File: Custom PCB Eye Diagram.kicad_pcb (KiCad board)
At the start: 4 copper layers, 82.8 x 100.2 mm, 49 parts, among them IC1 CLK DSC1123CI2-125.0000, J1 RD53 Data Lines DP 47272-0001, J10 JTAG Connector 0878321420, J11 12v Input PJ-102B, J12 LVDS Pair-P Conn_01x02, J13 LVDS Pair-N Conn_01x02, J14 MGT CLK-P Conn_01x01, J15 MGT CLK-N Conn_01x01, J16 Ground Pin Conn_01x04, J17 Ground Pins Conn_01x04, J2 Conn_01x02, J3 LSHM-1 LSHM-150-XX.X-XX-DV-A-N, J4 Loopback DP 47272-0001, J5 LSHM-2 LSHM-150-XX.X-XX-DV-A-N, J6 Vin Conn_01x03, J7 Conn_01x02, J8 LVDS-N Conn_01x02, J9 LVDS-P Conn_01x02, U1 DCDC Convertor 12v to 3.3v OKI-78SR-3.3_1.5-W36-C

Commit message: Added test LEDs for practicing FPGA programming
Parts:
- added D2: LED, LED_SMD:LED_0603_1608Metric, F.Cu at (147.3, 97.6)
- added D3: LED, LED_SMD:LED_0603_1608Metric, F.Cu at (143.8, 79.2)
- added D4: LED, LED_SMD:LED_0603_1608Metric, F.Cu at (146.8, 79.1)
- added R5: R, Resistor_SMD:R_0402_1005Metric, F.Cu at (147.3, 93.9)
- added R6: R, Resistor_SMD:R_0402_1005Metric, F.Cu at (143.8, 83.5)
- added R7: R, Resistor_SMD:R_0402_1005Metric, F.Cu at (146.8, 82.3)
- C7: renamed from C7 VIn
- D1: renamed from D1 Power Light
- IC1: renamed from IC1 CLK
- J1: renamed from J1 RD53 Data Lines DP
- J10: renamed from J10 JTAG Connector
- J11: renamed from J11 12v Input
- J12: renamed from J12 LVDS Pair-P
- J13: renamed from J13 LVDS Pair-N
- J14: renamed from J14 MGT CLK-P
- J15: renamed from J15 MGT CLK-N
- J16: renamed from J16 Ground Pin
- J17: renamed from J17 Ground Pins
- J3: renamed from J3 LSHM-1
- J4: renamed from J4 Loopback DP
- J5: renamed from J5 LSHM-2
- J6: renamed from J6 Vin
- J8: renamed from J8 LVDS-N
- J9: renamed from J9 LVDS-P
- U1: renamed from U1 DCDC Convertor 12v to 3.3v
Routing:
- net GND: track 96.0 -> 102.0 mm, vias 15 -> 18
- net Net-(J3-Pad56): track 0.00 -> 3.83 mm
- net Net-(J3-Pad53): track 0.00 -> 3.12 mm
- net Net-(D3-Pad2): track 0.00 -> 3.03 mm
- net Net-(J3-Pad68): track 0.00 -> 2.64 mm
- net Net-(D2-Pad2): track 0.00 -> 2.42 mm
- net Net-(D4-Pad2): track 0.00 -> 1.89 mm

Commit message: Fixed test LED setup for FPGA programming practice
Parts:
- removed D2, D3, D4: LED, LED_SMD:LED_0603_1608Metric
- removed J7: Conn_01x02, Connector_PinHeader_2.54mm:PinHeader_1x02_P2.54mm_Vertical
- added 50 D2: LED, LED_SMD:LED_0603_1608Metric, F.Cu at (119.3, 72.0)
- added 56 D4: LED, LED_SMD:LED_0603_1608Metric, F.Cu at (119.3, 73.7)
- added 66 D9: LED, LED_SMD:LED_0603_1608Metric, F.Cu at (119.3, 75.5)
- added 68 D3: LED, LED_SMD:LED_0603_1608Metric, F.Cu at (119.3, 77.4)
- added 74 D5: LED, LED_SMD:LED_0603_1608Metric, F.Cu at (119.3, 79.1)
- added 78 D6: LED, LED_SMD:LED_0603_1608Metric, F.Cu at (119.3, 80.9)
- added 82 D7: LED, LED_SMD:LED_0603_1608Metric, F.Cu at (119.3, 82.5)
- added 88 D8: LED, LED_SMD:LED_0603_1608Metric, F.Cu at (119.2, 84.3)
- added J7 VIN: Conn_01x02, Connector_PinHeader_2.54mm:PinHeader_1x02_P2.54mm_Vertical, F.Cu at (202.6, 93.1)
- added R10: R, Resistor_SMD:R_0402_1005Metric, F.Cu at (140.8, 79.2)
- added R11: R, Resistor_SMD:R_0402_1005Metric, F.Cu at (139.7, 80.7)
- added R12: R, Resistor_SMD:R_0402_1005Metric, F.Cu at (138.3, 82.2)
- added R8: R, Resistor_SMD:R_0402_1005Metric, F.Cu at (143.8, 75.0)
- added R9: R, Resistor_SMD:R_0402_1005Metric, F.Cu at (141.8, 77.6)
- D1 Power LED: renamed from D1
- IC1 MGT_CLK circuit from FPGA: renamed from IC1
- J1 SCC GRX Signals: renamed from J1
- J10 JTAG Connector: renamed from J10
- J11 12v Power Input: renamed from J11
- J12 LVDS_P: renamed from J12
- J13 LVDS_N: renamed from J13
- J14 MGT_CLK_P: renamed from J14
- J15 MGT_CLK_N: renamed from J15
- J16 Ground Pins: renamed from J16
- J17 Ground Pins: renamed from J17
- J2 12v: renamed from J2
- J3 LSHM Connector to FPGA: renamed from J3
- J4 GTX Signals for Loopback: renamed from J4
- J5 Added for Stability: renamed from J5
- J6 VIN: renamed from J6
- J8 LVDS_N: renamed from J8
- J9 LVDS_P: renamed from J9
- U1 12v to 3.3v DCDC Converter: renamed from U1
- moved J16 Ground Pins 30.5 mm to (172.1, 147.1)
- moved R5 21.9 mm to (147.8, 72.0), turned to 180 degrees
- moved R7 8.73 mm to (146.2, 73.6), turned to 0 degrees
- moved J11 12v Power Input 7.76 mm to (120.3, 124.9)
- moved R6 7.02 mm to (143.0, 76.5), turned to 0 degrees
- moved REF** 6.50 mm to (121.6, 145.7)
- moved REF** 6.50 mm to (121.6, 55.5)
- moved C7 4.80 mm to (129.2, 86.0)
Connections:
- FB1 pad 2: +3V3 -> /VIN
- R5 pad 1: Net-(J3-Pad53) -> Net-(J3-Pad50)
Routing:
- net Net-(D2-Pad2): track 2.42 -> 27.3 mm
- net Net-(D4-Pad2): track 1.89 -> 25.8 mm
- net Net-(D9-Pad2): track 0.00 -> 23.4 mm
- net Net-(D5-Pad2): track 0.00 -> 21.9 mm
- net Net-(D6-Pad2): track 0.00 -> 20.9 mm
- net Net-(D7-Pad2): track 0.00 -> 19.9 mm
- net Net-(D3-Pad2): track 3.03 -> 22.8 mm
- net Net-(D8-Pad2): track 0.00 -> 18.6 mm
- net Net-(J3-Pad50): track 0.00 -> 14.7 mm
- net Net-(J3-Pad66): track 0.00 -> 11.7 mm
- net GND: track 102.0 -> 111.5 mm, vias 18 -> 16
- net Net-(J3-Pad56): track 3.83 -> 13.1 mm
- net Net-(J3-Pad74): track 0.00 -> 8.96 mm
- net +12V: track 30.8 -> 38.5 mm
- net Net-(J3-Pad68): track 2.64 -> 10.2 mm
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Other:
- board size 82.8 x 100.2 mm -> 89.3 x 100.2 mm

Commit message: Added LBNL logo, name, and changed VIN layer to V3P3 layer
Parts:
- added G***: LOGO, lbnl_logo:lbnl_logo_large, F.Cu at (144.2, 144.7)
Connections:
- C7 pad 1: /VIN -> /V3P3
- C8 pad 2: /VIN -> /V3P3
- FB1 pad 2: /VIN -> /V3P3
- IC1 MGT_CLK circuit from FPGA pad 1: /VIN -> /V3P3
- J3 LSHM Connector to FPGA pad 100: /VIN -> /V3P3
- J3 LSHM Connector to FPGA pad 98: /VIN -> /V3P3
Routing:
- net /VIN: track 18.7 -> 0.00 mm, vias 3 -> 0
- net /V3P3: track 0.00 -> 18.7 mm, vias 0 -> 3
- added copper zone on In2.Cu, net /V3P3
- removed copper zone on In2.Cu, net /VIN
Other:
- board text added: "RD53B Digital Signal Eye Diagram PCB 1.0 Adam Molnar August 24 2020"

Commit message: Another iteration of the PCB and made some updates to the BOM
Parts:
- removed 50 D2: LED, LED_SMD:LED_0603_1608Metric
- removed 56 D4: LED, LED_SMD:LED_0603_1608Metric
- removed 66 D9: LED, LED_SMD:LED_0603_1608Metric
- removed 68 D3: LED, LED_SMD:LED_0603_1608Metric
- removed 74 D5: LED, LED_SMD:LED_0603_1608Metric
- removed 78 D6: LED, LED_SMD:LED_0603_1608Metric
- removed 82 D7: LED, LED_SMD:LED_0603_1608Metric
- removed 88 D8: LED, LED_SMD:LED_0603_1608Metric
- removed the C10 at (196.6, 108.5)
- removed the C6 at (198.9, 104.8)
- removed the C9 at (139.5, 129.4)
- removed D1 Power LED: LED, LED_SMD:LED_0603_1608Metric
- removed J11 12v Power Input: PJ-102B, PJ-102B:CUI_PJ-102B
- removed J14 MGT_CLK_P: Conn_01x01, Connector_PinHeader_2.54mm:PinHeader_1x01_P2.54mm_Vertical
- removed J15 MGT_CLK_N: Conn_01x01, Connector_PinHeader_2.54mm:PinHeader_1x01_P2.54mm_Vertical
- removed J16 Ground Pins: Conn_01x04, Connector_PinHeader_2.54mm:PinHeader_1x04_P2.54mm_Vertical
- removed J17 Ground Pins: Conn_01x04, Connector_PinHeader_2.54mm:PinHeader_1x04_P2.54mm_Vertical
- removed J2 12v: Conn_01x02, Connector_PinHeader_2.54mm:PinHeader_1x02_P2.54mm_Vertical
- removed J6 VIN: Conn_01x03, Connector_PinHeader_2.54mm:PinHeader_1x03_P2.54mm_Vertical
- removed the R3 at (176.6, 100.2)
- removed REF** (x4): MountingHole_3.2mm_M3, MountingHole:MountingHole_3.2mm_M3
- removed U1 12v to 3.3v DCDC Converter: OKI-78SR-3.3_1.5-W36-C, Converter_DCDC:Converter_DCDC_RECOM_R-78B-2.0_THT
- added 3.2mm: MountingHole_3.2mm_M3, MountingHole:MountingHole_3.2mm_M3, F.Cu at (200.8, 145.7)
- added 3.2mm : MountingHole_3.2mm_M3, MountingHole:MountingHole_3.2mm_M3, F.Cu at (120.6, 55.5)
- added 3.2mm: MountingHole_3.2mm_M3, MountingHole:MountingHole_3.2mm_M3, F.Cu at (200.8, 55.5)
- added 3.2mm: MountingHole_3.2mm_M3, MountingHole:MountingHole_3.2mm_M3, F.Cu at (120.6, 145.7)
- added C1: 10UF, Capacitor_SMD:C_0805_2012Metric, F.Cu at (150.2, 121.3)
- added C5: 10UF, Capacitor_SMD:C_0805_2012Metric, F.Cu at (131.6, 136.7)
- added C7: 470n, Capacitor_SMD:C_0805_2012Metric, F.Cu at (180.8, 108.0)
- added D1: LED, LED_SMD:LED_0603_1608Metric, F.Cu at (156.6, 129.0)
- added D2: LED, LED_SMD:LED_0603_1608Metric, F.Cu at (119.3, 79.1)
- added D3: LED, LED_SMD:LED_0603_1608Metric, F.Cu at (119.3, 80.9)
- added D4: LED, LED_SMD:LED_0603_1608Metric, F.Cu at (119.3, 82.5)
- added D5: LED, LED_SMD:LED_0603_1608Metric, F.Cu at (119.2, 84.3)
- added D6: LED, LED_SMD:LED_0603_1608Metric, F.Cu at (119.3, 72.0)
- added D7: LED, LED_SMD:LED_0603_1608Metric, F.Cu at (119.3, 77.4)
- added D8: LED, LED_SMD:LED_0603_1608Metric, F.Cu at (119.3, 73.7)
- added D9: LED, LED_SMD:LED_0603_1608Metric, F.Cu at (119.3, 75.5)
- added J1: Conn_01x02, Connector_PinHeader_2.54mm:PinHeader_1x02_P2.54mm_Vertical, F.Cu at (130.9, 118.8)
- added J10: PJ-102B, PJ-102B:CUI_PJ-102B, F.Cu at (118.2, 132.6)
- added J15: Conn_01x02, Connector_PinHeader_2.54mm:PinHeader_1x02_P2.54mm_Vertical, F.Cu at (168.7, 101.3)
- added J17: Conn_01x02, Connector_PinHeader_2.54mm:PinHeader_1x02_P2.54mm_Vertical, F.Cu at (158.6, 118.0)
- added J2: Conn_01x04, Connector_PinHeader_2.54mm:PinHeader_1x04_P2.54mm_Vertical, F.Cu at (172.1, 147.1)
- added J3: Conn_01x03, Connector_PinHeader_2.54mm:PinHeader_1x03_P2.54mm_Vertical, F.Cu at (143.9, 118.8)
- added J5: Conn_01x04, Connector_PinHeader_2.54mm:PinHeader_1x04_P2.54mm_Vertical, F.Cu at (145.2, 54.2)
- added R2: 200, Resistor_SMD:R_0603_1608Metric, F.Cu at (157.4, 124.8)
- added U1: OKI-78SR-3.3_1.5-W36-C, Converter_DCDC:Converter_DCDC_RECOM_R-78B-2.0_THT, F.Cu at (137.2, 134.1)
- C3: value 470n -> 10UF
- IC1: renamed from IC1 MGT_CLK circuit from FPGA
- J11: renamed from J12 LVDS_P
- J12: renamed from J13 LVDS_N
- J13: renamed from J4 GTX Signals for Loopback
- J14: renamed from J3 LSHM Connector to FPGA
- J16: renamed from J5 Added for Stability
- J4: renamed from J7 VIN
- J6: renamed from J10 JTAG Connector
- J7: renamed from J9 LVDS_P
- J8: renamed from J8 LVDS_N
- J9: renamed from J1 SCC GRX Signals
- R4: value 200 -> 100
- moved J4 69.2 mm to (137.4, 116.3)
- moved F1 50.0 mm to (150.2, 117.1)
- moved L1 49.4 mm to (153.7, 118.7)
- moved C3 45.1 mm to (153.7, 125.0), turned to 270 degrees
- moved R4 24.8 mm to (177.4, 100.4)
- moved G*** 15.2 mm to (159.1, 141.6)
- moved C6 13.5 mm to (185.7, 99.3), turned to 180 degrees
- moved FB1 9.26 mm to (181.1, 105.1), turned to 0 degrees
- moved IC1 6.85 mm to (180.8, 100.7), turned to 90 degrees
- moved J6 6.75 mm to (138.1, 103.8), turned to 0 degrees
- moved J12 2.94 mm to (170.1, 133.9)
- moved J11 2.88 mm to (170.1, 130.3)
- moved C9 2.85 mm to (174.0, 99.6)
- moved C8 2.53 mm to (174.0, 100.6)
- moved C18 2.16 mm to (171.5, 69.8)
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- renumbered C7 to C10, C18 to C11, C13 to C12, C12 to C13, C11 to C14, C14 to C18, C1 to C2, C2 to C4, C8 to C6, C4 to C8, C5 to C9, R5 to R10, R6 to R11, R7 to R12, R2 to R3, R8 to R5, R9 to R6, R10 to R7, R11 to R8, R12 to R9
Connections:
- net Net-(C11-Pad1) renamed /MGT_RX0_C_P
- net Net-(C12-Pad1) renamed /MGT_RX0_C_N
- net Net-(C13-Pad1) renamed /MGT_RX3_C_P
- net Net-(C14-Pad1) renamed /MGT_RX1_C_N
- net Net-(C15-Pad1) renamed /MGT_RX1_C_P
- net Net-(C16-Pad1) renamed /MGT_RX2_C_N
- net Net-(C17-Pad1) renamed /MGT_RX2_C_P
- net Net-(C18-Pad2) renamed /MGT_RX3_C_N
- net Net-(F1-Pad2) renamed /V3P3RAW
- net Net-(J1-Pad15) renamed /LVDS_0_J_P
- net Net-(J1-Pad17) renamed /LVDS_0_J_N
- net Net-(J12-Pad2) renamed /LVDS_1_J_P
- net Net-(J13-Pad2) renamed /LVDS_1_J_N
- C10 pad 1: /V3P3 -> +3V3
- C3 pad 1: GND -> +3V3
- C3 pad 2: Net-(C3-Pad2) -> GND
- C6 pad 2: /V3P3 -> +3V3
- C8 pad 2: Net-(C4-Pad2) -> /MGT_CLK_C_P
- C9 pad 2: Net-(C5-Pad2) -> /MGT_CLK_C_N
- FB1 pad 1: Net-(C3-Pad2) -> Net-(C7-Pad2)
- FB1 pad 2: /V3P3 -> +3V3
- IC1 pad 1: /V3P3 -> +3V3
- IC1 pad 2: Net-(IC1-Pad2) -> (no net)
- IC1 pad 4: Net-(C5-Pad2) -> /MGT_CLK_C_N
- IC1 pad 5: Net-(C4-Pad2) -> /MGT_CLK_C_P
- IC1 pad 6: Net-(C3-Pad2) -> Net-(C7-Pad2)
- J13 pad 13: Net-(J4-Pad13) -> (no net)
- J13 pad 14: Net-(J4-Pad14) -> (no net)
- J13 pad 18: Net-(J4-Pad18) -> (no net)
- J13 pad 19: Net-(J4-Pad19) -> (no net)
- J13 pad 20: Net-(J4-Pad20) -> (no net)
- J14 pad 1: /MGT_CLK0_P -> /MGT_CLK0_N
- J14 pad 100: /V3P3 -> +3V3
- J14 pad 26: Net-(J3-Pad26) -> (no net)
- J14 pad 28: Net-(J3-Pad28) -> (no net)
- J14 pad 3: /MGT_CLK0_N -> /MGT_CLK0_P
- J14 pad 30: Net-(J3-Pad30) -> (no net)
- J14 pad 32: /LVDS_0_P -> /LVDS_0_N
- J14 pad 34: /LVDS_0_N -> /LVDS_0_P
- J14 pad 35: Net-(J3-Pad35) -> (no net)
- J14 pad 36: Net-(J3-Pad36) -> (no net)
- J14 pad 37: Net-(J3-Pad37) -> (no net)
- J14 pad 38: Net-(J3-Pad38) -> (no net)
- J14 pad 39: Net-(J3-Pad39) -> (no net)
- J14 pad 40: Net-(J3-Pad40) -> (no net)
- J14 pad 41: Net-(J3-Pad41) -> (no net)
- J14 pad 42: Net-(J3-Pad42) -> (no net)
- J14 pad 43: Net-(J3-Pad43) -> (no net)
- J14 pad 44: Net-(J3-Pad44) -> (no net)
- J14 pad 45: Net-(J3-Pad45) -> (no net)
- J14 pad 46: Net-(J3-Pad46) -> (no net)
- J14 pad 49: Net-(J3-Pad49) -> (no net)
- J14 pad 51: Net-(J3-Pad51) -> (no net)
- J14 pad 52: Net-(J3-Pad52) -> (no net)
- J14 pad 53: Net-(J3-Pad53) -> (no net)
- J14 pad 54: Net-(J3-Pad54) -> (no net)
- J14 pad 55: Net-(J3-Pad55) -> (no net)
- J14 pad 57: Net-(J3-Pad57) -> (no net)
- J14 pad 58: Net-(J3-Pad58) -> (no net)
- J14 pad 59: Net-(J3-Pad59) -> (no net)
- J14 pad 60: Net-(J3-Pad60) -> (no net)
- J14 pad 61: Net-(J3-Pad61) -> (no net)
- J14 pad 62: Net-(J3-Pad62) -> (no net)
- J14 pad 63: Net-(J3-Pad63) -> (no net)
- J14 pad 64: Net-(J3-Pad64) -> (no net)
- J14 pad 65: Net-(J3-Pad65) -> (no net)
- J14 pad 67: Net-(J3-Pad67) -> (no net)
- J14 pad 69: Net-(J3-Pad69) -> (no net)
- J14 pad 70: Net-(J3-Pad70) -> (no net)
- J14 pad 71: Net-(J3-Pad71) -> (no net)
- J14 pad 72: Net-(J3-Pad72) -> (no net)
- J14 pad 73: Net-(J3-Pad73) -> (no net)
- J14 pad 75: Net-(J3-Pad75) -> (no net)
- J14 pad 76: Net-(J3-Pad76) -> (no net)
- J14 pad 77: Net-(J3-Pad77) -> (no net)
- J14 pad 79: Net-(J3-Pad79) -> (no net)
- J14 pad 80: Net-(J3-Pad80) -> (no net)
- J14 pad 81: Net-(J3-Pad81) -> (no net)
- J14 pad 84: Net-(J3-Pad84) -> (no net)
- J14 pad 86: Net-(J3-Pad86) -> (no net)
- J14 pad 90: Net-(J3-Pad90) -> (no net)
- J14 pad 92: Net-(J3-Pad92) -> (no net)
- J14 pad 93: Net-(J3-Pad93) -> (no net)
- J14 pad 94: Net-(J3-Pad94) -> (no net)
- J14 pad 95: Net-(J3-Pad95) -> (no net)
- J14 pad 96: Net-(J3-Pad96) -> (no net)
- J14 pad 98: /V3P3 -> +3V3
- J16 pad 1: Net-(J5-Pad1) -> (no net)
- J16 pad 10: Net-(J5-Pad10) -> (no net)
- J16 pad 100: Net-(J5-Pad100) -> (no net)
- J16 pad 11: Net-(J5-Pad11) -> (no net)
- J16 pad 12: Net-(J5-Pad12) -> (no net)
- J16 pad 13: Net-(J5-Pad13) -> (no net)
- J16 pad 14: Net-(J5-Pad14) -> (no net)
- J16 pad 15: Net-(J5-Pad15) -> (no net)
- J16 pad 16: Net-(J5-Pad16) -> (no net)
- J16 pad 17: Net-(J5-Pad17) -> (no net)
- J16 pad 18: Net-(J5-Pad18) -> (no net)
- J16 pad 19: Net-(J5-Pad19) -> (no net)
- J16 pad 2: Net-(J5-Pad2) -> (no net)
- J16 pad 20: Net-(J5-Pad20) -> (no net)
- J16 pad 21: Net-(J5-Pad21) -> (no net)
- J16 pad 22: Net-(J5-Pad22) -> (no net)
- J16 pad 23: Net-(J5-Pad23) -> (no net)
- J16 pad 24: Net-(J5-Pad24) -> (no net)
- J16 pad 25: Net-(J5-Pad25) -> (no net)
- J16 pad 26: Net-(J5-Pad26) -> (no net)
- J16 pad 27: Net-(J5-Pad27) -> (no net)
- J16 pad 28: Net-(J5-Pad28) -> (no net)
- J16 pad 29: Net-(J5-Pad29) -> (no net)
- J16 pad 3: Net-(J5-Pad3) -> (no net)
- J16 pad 30: Net-(J5-Pad30) -> (no net)
- J16 pad 31: Net-(J5-Pad31) -> (no net)
- J16 pad 32: Net-(J5-Pad32) -> (no net)
- J16 pad 33: Net-(J5-Pad33) -> (no net)
- J16 pad 34: Net-(J5-Pad34) -> (no net)
- J16 pad 35: Net-(J5-Pad35) -> (no net)
- J16 pad 36: Net-(J5-Pad36) -> (no net)
- J16 pad 37: Net-(J5-Pad37) -> (no net)
- J16 pad 38: Net-(J5-Pad38) -> (no net)
- J16 pad 39: Net-(J5-Pad39) -> (no net)
- J16 pad 4: Net-(J5-Pad4) -> (no net)
- J16 pad 40: Net-(J5-Pad40) -> (no net)
- J16 pad 41: Net-(J5-Pad41) -> (no net)
- J16 pad 42: Net-(J5-Pad42) -> (no net)
- J16 pad 43: Net-(J5-Pad43) -> (no net)
- J16 pad 44: Net-(J5-Pad44) -> (no net)
- J16 pad 45: Net-(J5-Pad45) -> (no net)
- J16 pad 46: Net-(J5-Pad46) -> (no net)
- J16 pad 47: Net-(J5-Pad47) -> (no net)
- J16 pad 48: Net-(J5-Pad48) -> (no net)
- J16 pad 49: Net-(J5-Pad49) -> (no net)
- J16 pad 5: Net-(J5-Pad5) -> (no net)
- J16 pad 50: Net-(J5-Pad50) -> (no net)
- J16 pad 51: Net-(J5-Pad51) -> (no net)
- J16 pad 52: Net-(J5-Pad52) -> (no net)
- J16 pad 53: Net-(J5-Pad53) -> (no net)
- J16 pad 54: Net-(J5-Pad54) -> (no net)
- J16 pad 55: Net-(J5-Pad55) -> (no net)
- J16 pad 56: Net-(J5-Pad56) -> (no net)
- J16 pad 57: Net-(J5-Pad57) -> (no net)
- J16 pad 58: Net-(J5-Pad58) -> (no net)
- J16 pad 59: Net-(J5-Pad59) -> (no net)
- J16 pad 6: Net-(J5-Pad6) -> (no net)
- J16 pad 60: Net-(J5-Pad60) -> (no net)
- J16 pad 61: Net-(J5-Pad61) -> (no net)
- J16 pad 62: Net-(J5-Pad62) -> (no net)
- J16 pad 63: Net-(J5-Pad63) -> (no net)
- J16 pad 64: Net-(J5-Pad64) -> (no net)
- J16 pad 65: Net-(J5-Pad65) -> (no net)
- J16 pad 66: Net-(J5-Pad66) -> (no net)
- J16 pad 67: Net-(J5-Pad67) -> (no net)
- J16 pad 68: Net-(J5-Pad68) -> (no net)
- J16 pad 69: Net-(J5-Pad69) -> (no net)
- J16 pad 7: Net-(J5-Pad7) -> (no net)
- J16 pad 70: Net-(J5-Pad70) -> (no net)
- J16 pad 71: Net-(J5-Pad71) -> (no net)
- J16 pad 72: Net-(J5-Pad72) -> (no net)
- J16 pad 73: Net-(J5-Pad73) -> (no net)
- J16 pad 74: Net-(J5-Pad74) -> (no net)
- J16 pad 75: Net-(J5-Pad75) -> (no net)
- J16 pad 76: Net-(J5-Pad76) -> (no net)
- J16 pad 77: Net-(J5-Pad77) -> (no net)
- J16 pad 78: Net-(J5-Pad78) -> (no net)
- J16 pad 79: Net-(J5-Pad79) -> (no net)
- J16 pad 8: Net-(J5-Pad8) -> (no net)
- J16 pad 80: Net-(J5-Pad80) -> (no net)
- J16 pad 81: Net-(J5-Pad81) -> (no net)
- J16 pad 82: Net-(J5-Pad82) -> (no net)
- J16 pad 83: Net-(J5-Pad83) -> (no net)
- J16 pad 84: Net-(J5-Pad84) -> (no net)
- J16 pad 85: Net-(J5-Pad85) -> (no net)
- J16 pad 86: Net-(J5-Pad86) -> (no net)
- J16 pad 87: Net-(J5-Pad87) -> (no net)
- J16 pad 88: Net-(J5-Pad88) -> (no net)
- J16 pad 89: Net-(J5-Pad89) -> (no net)
- J16 pad 9: Net-(J5-Pad9) -> (no net)
- J16 pad 90: Net-(J5-Pad90) -> (no net)
- J16 pad 91: Net-(J5-Pad91) -> (no net)
- J16 pad 92: Net-(J5-Pad92) -> (no net)
- J16 pad 93: Net-(J5-Pad93) -> (no net)
- J16 pad 94: Net-(J5-Pad94) -> (no net)
- J16 pad 95: Net-(J5-Pad95) -> (no net)
- J16 pad 96: Net-(J5-Pad96) -> (no net)
- J16 pad 97: Net-(J5-Pad97) -> (no net)
- J16 pad 98: Net-(J5-Pad98) -> (no net)
- J16 pad 99: Net-(J5-Pad99) -> (no net)
- J6 pad 12: Net-(J10-Pad12) -> (no net)
- J6 pad 14: Net-(J10-Pad14) -> (no net)
- J6 pad 2: Net-(J10-Pad2) -> (no net)
- J9 pad 13: Net-(J1-Pad13) -> (no net)
- J9 pad 14: Net-(J1-Pad14) -> (no net)
- J9 pad 18: Net-(J1-Pad18) -> (no net)
- J9 pad 19: Net-(J1-Pad19) -> (no net)
- J9 pad 20: Net-(J1-Pad20) -> (no net)
- L1 pad 2: Net-(C10-Pad1) -> +3V3
- R4 pad 1: Net-(C10-Pad1) -> /MGT_CLK_C_N
- R4 pad 2: Net-(D1-Pad2) -> /MGT_CLK_C_P
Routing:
- net +3V3: track 0.00 -> 37.4 mm, vias 0 -> 8
- net Net-(C5-Pad2): track 32.3 -> 0.00 mm
- net GND: track 111.5 -> 91.8 mm, vias 16 -> 41
- net /V3P3: track 18.7 -> 0.00 mm, vias 3 -> 0
- net Net-(C4-Pad2): track 15.3 -> 0.00 mm
- net /DCV3P3: track 0.00 -> 13.7 mm
- net Net-(C3-Pad2): track 13.3 -> 0.00 mm
- net /LVDS_0_P: track 20.8 -> 31.8 mm
- net /LVDS_0_N: track 20.7 -> 31.3 mm
- net /MGT_TX0_N: track 68.5 -> 60.2 mm
- net /MGT_TX0_P: track 67.6 -> 59.7 mm
- net Net-(C1-Pad1): track 13.7 -> 6.09 mm
- net /MGT_TX1_N: track 65.7 -> 58.1 mm
- net Net-(C10-Pad1): track 7.54 -> 0.00 mm
- net /MGT_TX1_P: track 64.8 -> 57.7 mm
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- added copper zone on F.Cu, net +3V3
- added copper zone on In2.Cu, net +3V3
- removed copper zone on In2.Cu, net /V3P3
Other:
- board size 89.3 x 100.2 mm -> 90.3 x 100.2 mm
- net class Default: clearance 0.2 -> 0.125
- rule trace_clearance: 0.2 -> 0.125
- board text added: "+12V"
- board text added: "12V Power Input"
- board text added: "12V to 3.3V DCDC Converter"
- board text added: "50"
- board text added: "56"
- board text added: "66"
- board text added: "68"
- board text added: "74"
- board text added: "78"
- board text added: "82"
- board text added: "88"
- board text added: "GTX Signals for Loopback"
- board text added: "Ground Pins"
- board text added: "JTAG Connector"
- board text added: "LSHM Connector Added for Stability"
- board text added: "LSHM Connector to FPGA"
- board text added: "LVDS_N"
- board text added: "LVDS_P"
- board text added: "MGT_CLK Circuit from FPGA"
- board text added: "MGT_CLK0_N"
- board text added: "MGT_CLK_P"
- board text added: "Power LED"
- board text added: "SCC GRX Signals"
- board text added: "V3P3"
- board text added: "V3P3RAW"
- board text added: "V3P3RAW Voltage Selector"

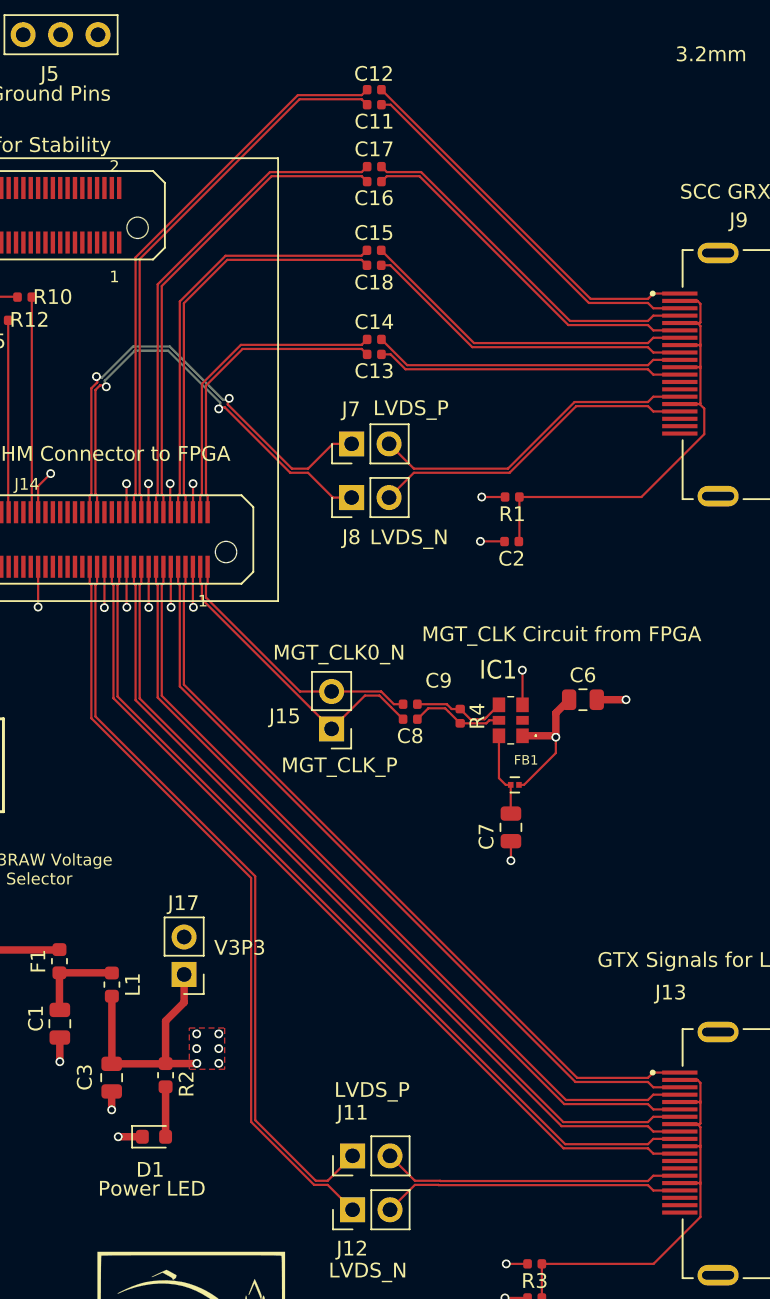
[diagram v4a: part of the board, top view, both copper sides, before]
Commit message: Changed the trace width and trace spacing to the proper values needed for impedance matching
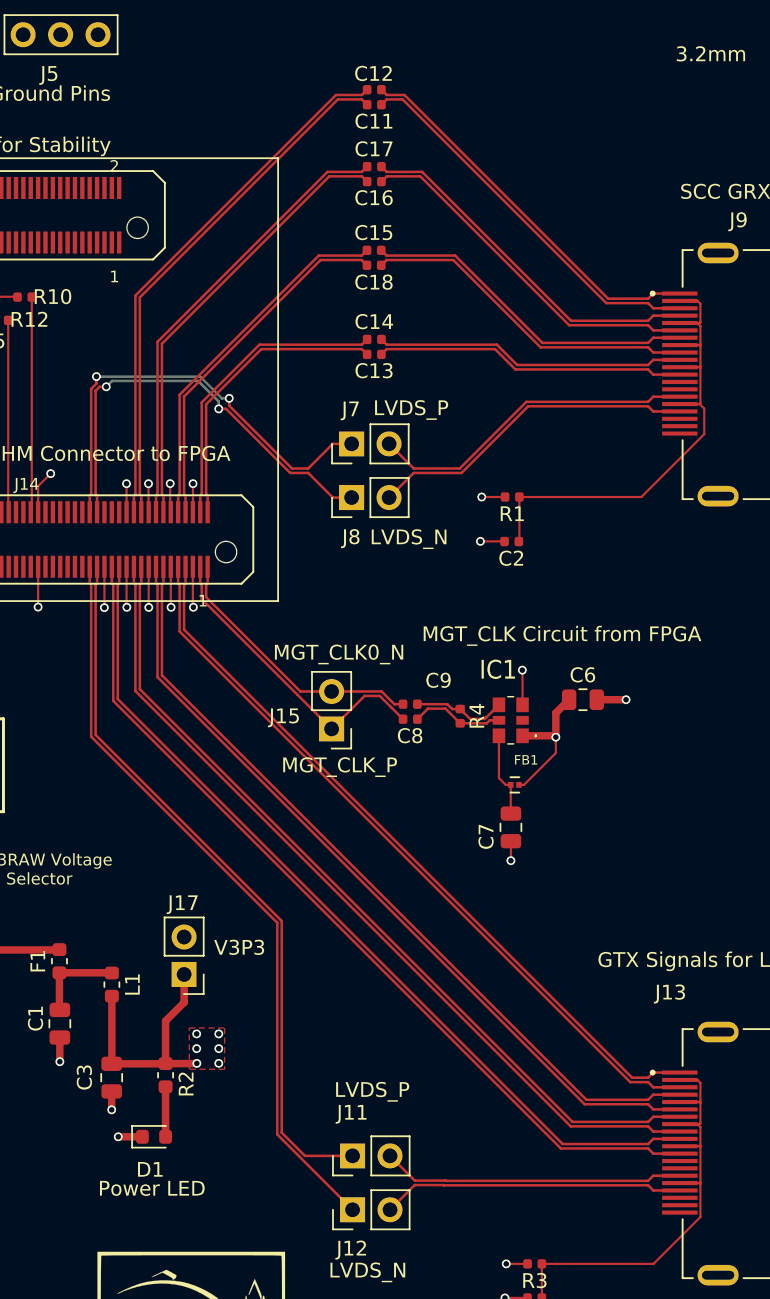
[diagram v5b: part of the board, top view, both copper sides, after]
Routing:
- net /MGT_RX1_C_N: track 28.0 -> 24.3 mm
- net /MGT_RX1_C_P: track 28.5 -> 24.8 mm
- net /MGT_RX2_C_N: track 32.6 -> 30.3 mm
- net /MGT_RX2_C_P: track 33.0 -> 30.7 mm
- net /MGT_TX3_P: track 52.9 -> 50.7 mm
- net /MGT_TX3_N: track 53.4 -> 51.2 mm
- net /LVDS_1_P: track 51.1 -> 49.1 mm
- net /LVDS_0_N: track 31.3 -> 29.5 mm
- net /MGT_RX3_C_N: track 37.3 -> 35.8 mm
- net /LVDS_0_P: track 31.8 -> 30.3 mm
- net /MGT_RX3_C_P: track 37.8 -> 36.3 mm
- net /MGT_TX2_P: track 55.5 -> 54.6 mm
- net /MGT_TX2_N: track 55.9 -> 55.1 mm
- net /MGT_RX0_C_N: track 20.8 -> 20.0 mm
- net /MGT_RX0_C_P: track 21.2 -> 20.5 mm
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
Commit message: PCB 2.0
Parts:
- moved J11 53.4 mm to (170.1, 76.9)
- moved J12 53.4 mm to (170.1, 80.6)
- moved J13 52.9 mm to (205.8, 77.3)
- moved R3 52.9 mm to (182.4, 84.8)
- moved C4 52.8 mm to (182.4, 87.1)
- moved C12 52.3 mm to (171.6, 110.2)
- moved C13 52.3 mm to (171.6, 128.2)
- moved C14 52.3 mm to (171.6, 127.2)
- moved C17 52.3 mm to (171.6, 115.4)
- moved C18 52.3 mm to (171.5, 122.1)
- moved J8 52.3 mm to (170.0, 137.9)
- moved J9 52.3 mm to (205.8, 129.6)
- moved C11 52.3 mm to (171.6, 111.2)
- moved C15 52.3 mm to (171.5, 121.1)
- moved C16 52.3 mm to (171.6, 116.5)
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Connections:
- J14 pad 1: /MGT_CLK0_N -> (no net)
- J14 pad 10: /MGT_RX1_C_P -> (no net)
- J14 pad 100: +3V3 -> (no net)
- J14 pad 11: GND -> (no net)
- J14 pad 12: GND -> (no net)
- J14 pad 13: /MGT_TX2_P -> (no net)
- J14 pad 14: /MGT_RX2_C_N -> (no net)
- J14 pad 15: /MGT_TX2_N -> (no net)
- J14 pad 16: /MGT_RX2_C_P -> (no net)
- J14 pad 17: GND -> (no net)
- J14 pad 18: GND -> (no net)
- J14 pad 19: /MGT_TX1_P -> (no net)
- J14 pad 2: /MGT_RX0_C_N -> (no net)
- J14 pad 20: /MGT_RX3_C_N -> (no net)
- J14 pad 21: /MGT_TX1_N -> (no net)
- J14 pad 22: /MGT_RX3_C_P -> (no net)
- J14 pad 23: GND -> (no net)
- J14 pad 24: GND -> (no net)
- J14 pad 25: /MGT_TX0_P -> (no net)
- J14 pad 27: /MGT_TX0_N -> (no net)
- J14 pad 29: GND -> (no net)
- J14 pad 3: /MGT_CLK0_P -> (no net)
- J14 pad 31: /LVDS_1_P -> (no net)
- J14 pad 32: /LVDS_0_N -> (no net)
- J14 pad 33: /LVDS_1_N -> (no net)
- J14 pad 34: /LVDS_0_P -> (no net)
- J14 pad 4: /MGT_RX0_C_P -> (no net)
- J14 pad 47: GND -> (no net)
- J14 pad 48: GND -> (no net)
- J14 pad 5: GND -> (no net)
- J14 pad 50: Net-(J14-Pad50) -> (no net)
- J14 pad 56: Net-(J14-Pad56) -> (no net)
- J14 pad 6: GND -> (no net)
- J14 pad 66: Net-(J14-Pad66) -> (no net)
- J14 pad 68: Net-(J14-Pad68) -> (no net)
- J14 pad 7: /MGT_TX3_P -> (no net)
- J14 pad 74: Net-(J14-Pad74) -> (no net)
- J14 pad 78: Net-(J14-Pad78) -> (no net)
- J14 pad 8: /MGT_RX1_C_N -> (no net)
- J14 pad 82: Net-(J14-Pad82) -> (no net)
- J14 pad 83: GND -> (no net)
- J14 pad 85: /TDI -> (no net)
- J14 pad 87: /TDO -> (no net)
- J14 pad 88: Net-(J14-Pad88) -> (no net)
- J14 pad 89: /TCK -> (no net)
- J14 pad 9: /MGT_TX3_N -> (no net)
- J14 pad 91: /TMS -> (no net)
- J14 pad 97: GND -> (no net)
- J14 pad 98: +3V3 -> (no net)
- J14 pad 99: GND -> (no net)
- J16 pad 1: (no net) -> /MGT_RX3_C_P
- J16 pad 10: (no net) -> /MGT_TX0_P
- J16 pad 100: (no net) -> GND
- J16 pad 11: (no net) -> GND
- J16 pad 12: (no net) -> GND
- J16 pad 13: (no net) -> /MGT_RX1_C_P
- J16 pad 14: (no net) -> /MGT_TX1_N
- J16 pad 15: (no net) -> /MGT_RX1_C_N
- J16 pad 16: (no net) -> /MGT_TX1_P
- J16 pad 17: (no net) -> GND
- J16 pad 18: (no net) -> GND
- J16 pad 19: (no net) -> /MGT_RX0_C_P
- J16 pad 2: (no net) -> /MGT_CLK0_P
- J16 pad 20: (no net) -> /MGT_TX2_N
- J16 pad 21: (no net) -> /MGT_RX0_C_N
- J16 pad 22: (no net) -> /MGT_TX2_P
- J16 pad 23: (no net) -> GND
- J16 pad 24: (no net) -> GND
- J16 pad 26: (no net) -> /MGT_TX3_N
- J16 pad 28: (no net) -> /MGT_TX3_P
- J16 pad 29: (no net) -> GND
- J16 pad 3: (no net) -> /MGT_RX3_C_N
- J16 pad 30: (no net) -> GND
- J16 pad 31: (no net) -> /LVDS_0_P
- J16 pad 32: (no net) -> /LVDS_1_N
- J16 pad 33: (no net) -> /LVDS_0_N
- J16 pad 34: (no net) -> /LVDS_1_P
- J16 pad 4: (no net) -> /MGT_CLK0_N
- J16 pad 47: (no net) -> GND
- J16 pad 48: (no net) -> GND
- J16 pad 49: (no net) -> Net-(J16-Pad49)
- J16 pad 5: (no net) -> GND
- J16 pad 55: (no net) -> Net-(J16-Pad55)
- J16 pad 6: (no net) -> GND
- J16 pad 65: (no net) -> Net-(J16-Pad65)
- J16 pad 66: (no net) -> GND
- J16 pad 67: (no net) -> Net-(J16-Pad67)
- J16 pad 7: (no net) -> /MGT_RX2_C_P
- J16 pad 73: (no net) -> Net-(J16-Pad73)
- J16 pad 77: (no net) -> Net-(J16-Pad77)
- J16 pad 8: (no net) -> /MGT_TX0_N
- J16 pad 81: (no net) -> Net-(J16-Pad81)
- J16 pad 84: (no net) -> GND
- J16 pad 86: (no net) -> /TDI
- J16 pad 87: (no net) -> Net-(J16-Pad87)
- J16 pad 88: (no net) -> /TDO
- J16 pad 9: (no net) -> /MGT_RX2_C_N
- J16 pad 90: (no net) -> /TCK
- J16 pad 92: (no net) -> /TMS
- J16 pad 97: (no net) -> +3V3
- J16 pad 98: (no net) -> GND
- J16 pad 99: (no net) -> +3V3
- R10 pad 1: Net-(J14-Pad50) -> Net-(J16-Pad87)
- R11 pad 2: Net-(J14-Pad68) -> Net-(J16-Pad73)
- R12 pad 2: Net-(J14-Pad56) -> Net-(J16-Pad81)
- R5 pad 2: Net-(J14-Pad66) -> Net-(J16-Pad77)
- R6 pad 2: Net-(J14-Pad74) -> Net-(J16-Pad67)
- R7 pad 2: Net-(J14-Pad78) -> Net-(J16-Pad65)
- R8 pad 2: Net-(J14-Pad82) -> Net-(J16-Pad55)
- R9 pad 2: Net-(J14-Pad88) -> Net-(J16-Pad49)
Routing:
- net /LVDS_0_N: track 29.5 -> 75.3 mm, vias 2 -> 0
- net /MGT_RX0_C_N: track 20.0 -> 64.5 mm
- net /MGT_RX0_C_P: track 20.5 -> 63.9 mm
- net /LVDS_0_P: track 30.3 -> 73.4 mm, vias 2 -> 0
- net /MGT_CLK0_N: track 18.5 -> 53.5 mm
- net /MGT_CLK0_P: track 21.1 -> 55.2 mm
- net /MGT_RX1_C_N: track 24.3 -> 56.8 mm
- net /MGT_RX1_C_P: track 24.8 -> 56.0 mm
- net /MGT_RX2_C_N: track 30.3 -> 49.8 mm
- net /MGT_RX2_C_P: track 30.7 -> 49.0 mm
- net Net-(D6-Pad2): track 27.3 -> 11.8 mm
- net Net-(J14-Pad50): track 14.6 -> 0.00 mm
- net /LVDS_1_N: track 51.0 -> 37.0 mm, vias 0 -> 2
- net Net-(J16-Pad49): track 0.00 -> 13.9 mm
- net /MGT_TX0_N: track 60.3 -> 47.2 mm
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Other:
- outline, holes or cut-outs redrawn
- board text added: "49"
- board text added: "55"
- board text added: "65"
- board text added: "67"
- board text added: "73"
- board text added: "77"
- board text added: "81"
- board text added: "87"
- board text added: "RD53B Digital Signal Eye Diagram PCB 2.0 Adam Molnar December 11 2020"
- board text removed: "50"
- board text removed: "56"
- board text removed: "66"
- board text removed: "68"
- board text removed: "74"
- board text removed: "78"
- board text removed: "82"
- board text removed: "88"
- board text removed: "RD53B Digital Signal Eye Diagram PCB 1.0 Adam Molnar August 24 2020"
